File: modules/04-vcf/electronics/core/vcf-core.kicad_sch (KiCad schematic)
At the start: 7 parts, among them J1 Conn_01x06, J2 Conn_02x04_Counter_Clockwise, J3 Conn_02x02_Counter_Clockwise

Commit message: VCF JLCPCB verified for v1.0
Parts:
- H1, H2, H3, H4, J1, J2, J3: CHECKED YES -> (none)
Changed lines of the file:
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@@
 			)
 		)
-		(property "CHECKED" "YES"
+		(property "CHECKED" ""
 			(at 214.63 102.87 0)
 			(effects
@@
 			)
 		)
-		(property "CHECKED" "YES"
+		(property "CHECKED" ""
 			(at 255.27 101.6 0)
 			(effects
@@
 			)
 		)
-		(property "CHECKED" "YES"
+		(property "CHECKED" ""
 			(at 200.66 160.02 0)
 			(effects
@@
 			)
 		)
-		(property "CHECKED" "YES"
+		(property "CHECKED" ""
 			(at 179.07 160.02 0)
 			(effects
@@
 			)
 		)
-		(property "CHECKED" "YES"
+		(property "CHECKED" ""
 			(at 215.9 71.12 0)
 			(effects
@@
 			)
 		)
-		(property "CHECKED" "YES"
+		(property "CHECKED" ""
 			(at 220.98 160.02 0)
 			(effects
@@
 			)
 		)
-		(property "CHECKED" "YES"
+		(property "CHECKED" ""
 			(at 241.3 160.02 0)
 			(effects

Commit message: Added VCF full BOM
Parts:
- J1: CHECKED (none) -> YES; Part URL https://mou.sr/40bhVZG -> https://mou.sr/4puxA0F; Part no. 474-PRT-09280 -> 200-SSW10401TMS
- J2, J3: CHECKED (none) -> YES
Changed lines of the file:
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@@
 			)
 		)
-		(property "CHECKED" ""
+		(property "CHECKED" "YES"
 			(at 214.63 102.87 0)
 			(effects
@@
 			)
 		)
-		(property "CHECKED" ""
+		(property "CHECKED" "YES"
 			(at 255.27 101.6 0)
 			(effects
@@
 			)
 		)
-		(property "Part URL" "https://mou.sr/40bhVZG"
+		(property "Part URL" "https://mou.sr/4puxA0F"
 			(at 215.9 71.12 0)
 			(effects
@@
 			)
 		)
-		(property "CHECKED" ""
+		(property "CHECKED" "YES"
 			(at 215.9 71.12 0)
 			(effects
@@
 			)
 		)
-		(property "Part no." "474-PRT-09280"
-			(at 215.9 71.12 0)
-			(effects
+		(property "Part no." "200-SSW10401TMS"
+			(at 215.9 71.12 0)
+			(effects

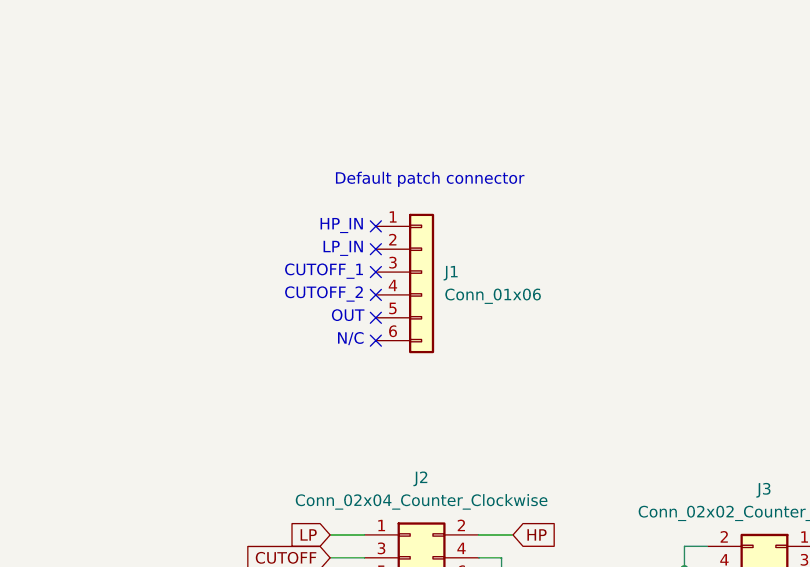
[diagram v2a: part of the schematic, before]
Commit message: Updated default pin to DNP in VCF core
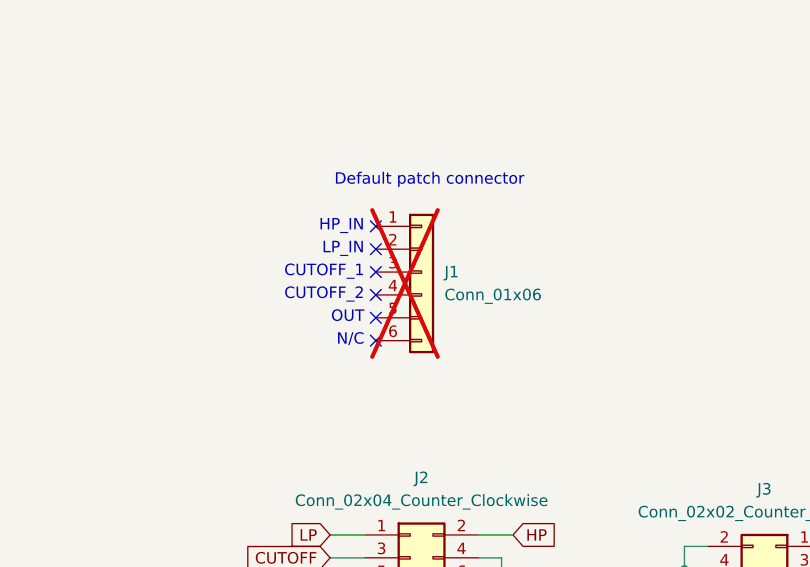
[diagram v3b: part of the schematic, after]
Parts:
- J1: now not fitted
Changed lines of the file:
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@@
 		(in_bom yes)
 		(on_board yes)
-		(dnp no)
+		(dnp yes)
 		(fields_autoplaced yes)
 		(property "Reference" "J1"
@@
 			(at 215.9 71.12 0)
 			(effects
+				(font
+					(size 1.27 1.27)
+				)
+				(hide yes)
+			)
+		)
+		(property "Part No." ""
+			(at 215.9 71.12 0)
+			(effects

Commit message: KiCAD version update - VCF
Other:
- title: Hog Moduleur VCF -> Moduleur VCF
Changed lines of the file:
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@@
 	(paper "A4")
 	(title_block
-		(title "Hog Moduleur VCF")
-		(date "2025-07-31")
-		(rev "v0.2")
+		(title "Moduleur VCF")
+		(date "2026-02-21")
+		(rev "v1.0")
 		(company "Shmøergh")
 	)
